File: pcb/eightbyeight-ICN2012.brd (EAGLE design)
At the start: 60 x 60 mm, 136 parts, among them CON1 USB_MICROSMT+THRUHULE, Q1 16MHz, SW1 SWITCH_SPDT, SW2 BRIGHTNESS, U1 MK20DN64VFM5, U2 ICN2026, U4 ICN2026, U5 MIC5219 3.3V, U6 ESP_WROOM_02, U8 MMA8653FC

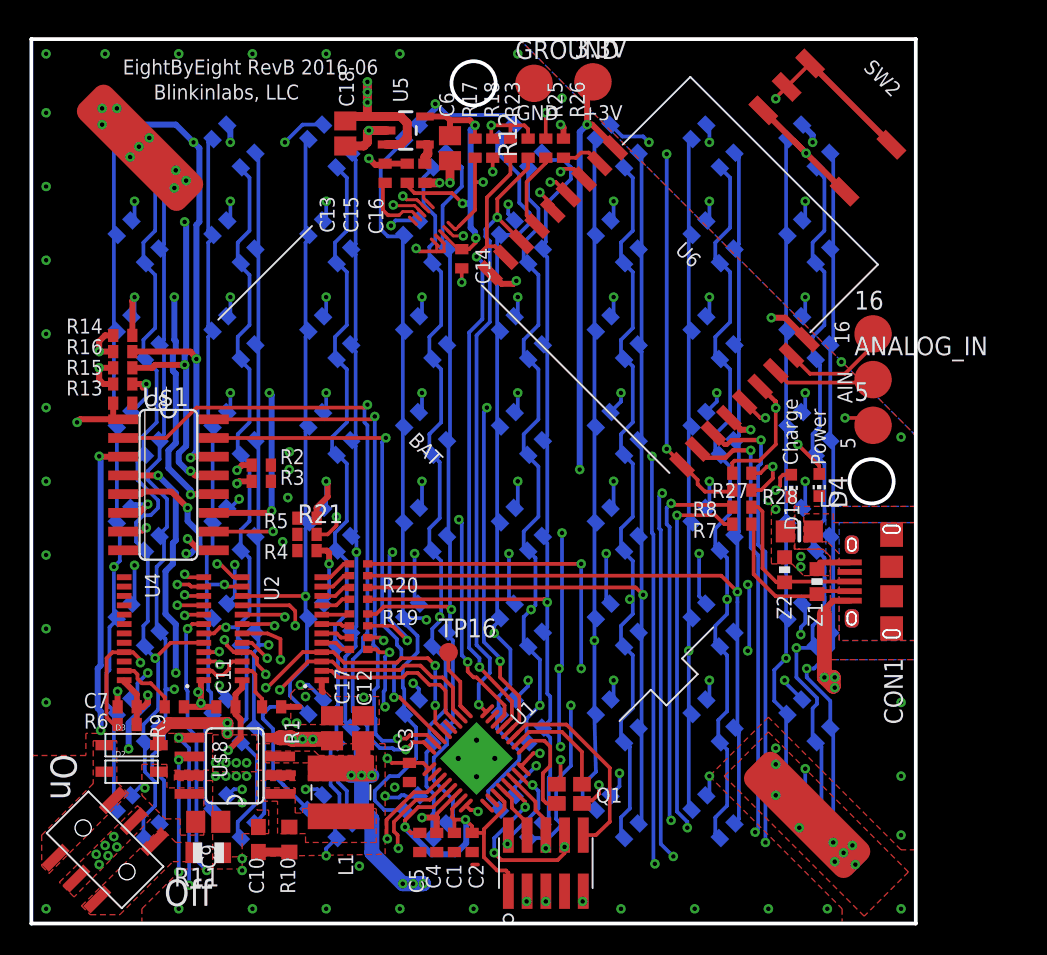
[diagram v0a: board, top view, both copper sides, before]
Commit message: Update ICN2012 version with new accelerometer
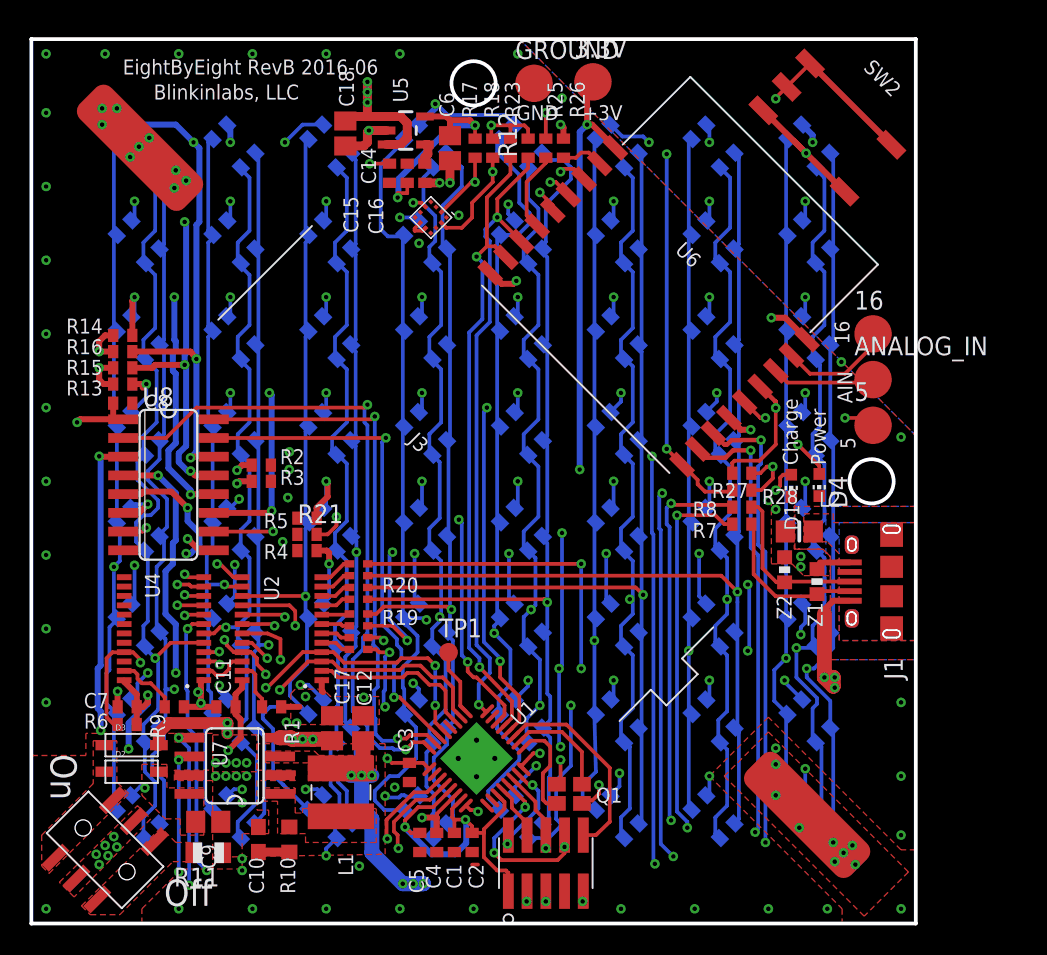
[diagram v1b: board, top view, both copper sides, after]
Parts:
- removed C13: 100nF, adafruit:C0402
- removed U$1: ICN2012, blinkinlabs:SO16
- added U3: QMA6981, DevicesToMerge:LGA2X2MM
- R21: value 2k 1% -> 10k
- U1: value MK20DN64VFM5 -> MK20DN32VFM5
- U8: value MMA8653FC -> ICN2012; device teensy_adapter:VFDFN-10 -> blinkinlabs:SO16
- moved U8 24.8 mm to (9.30, 30.4), turned to 270 degrees
- moved C14 7.59 mm to (24.3, 50.9), turned to 90 degrees
- renumbered BAT to J3, CON1 to J1, TP16 to TP1, U$2 to J2, U$8 to U7
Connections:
- removed net ACC_INT1: U6.IO13, U8.P$3
- removed net N$5: C13.1, U8.P$4
- new net ADC_INT1: U3.5, U6.IO13
- new net INT2: U3.6
- net +3V3: now also U3.3, U3.7; no longer U8.P$1, U8.P$8
- net +5V: now also U8.1, U8.9; no longer U$1.1, U$1.9
- net 1ROW0: now also U8.3; no longer U$1.3
- net 1ROW1: now also U8.4; no longer U$1.4
- net 1ROW2: now also U8.5; no longer U$1.5
- net 1ROW3: now also U8.6; no longer U$1.6
- net 1ROW4: now also U8.11; no longer U$1.11
- net 1ROW5: now also U8.12; no longer U$1.12
- net 1ROW6: now also U8.13; no longer U$1.13
- net 1ROW7: now also U8.14; no longer U$1.14
- net GND: now also U3.1, U3.4, U3.8, U3.9, U8.8; no longer C13.2, U$1.8, U8.P$6, U8.P$7, U8.P$9
- net I2C_SCL: now also U3.12; no longer U8.P$2
- net I2C_SDA: now also U3.2; no longer U8.P$10
- net LED_HS_EN: now also U8.7; no longer U$1.7
- net LED_OE: now also U8.10; no longer U$1.10
- net LED_ROW_A: now also U8.15; no longer U$1.15
- net LED_ROW_B: now also U8.16; no longer U$1.16
- net LED_ROW_C: now also U8.2; no longer U$1.2
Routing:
- net ACC_INT1: track 14.2 -> 0.00 mm, vias 2 -> 0
- net ADC_INT1: track 0.00 -> 11.4 mm, vias 0 -> 2
- net +3V3: track 83.2 -> 75.9 mm, vias 8 -> 7
- net N$5: track 4.61 -> 0.00 mm
- net GND: track 87.8 -> 90.7 mm, vias 90 -> 89
- net I2C_SCL: track 16.2 -> 13.7 mm, vias 3 -> 2
- net 1ROW6: track 82.9 -> 83.9 mm
- net I2C_SDA: track 12.5 -> 11.5 mm

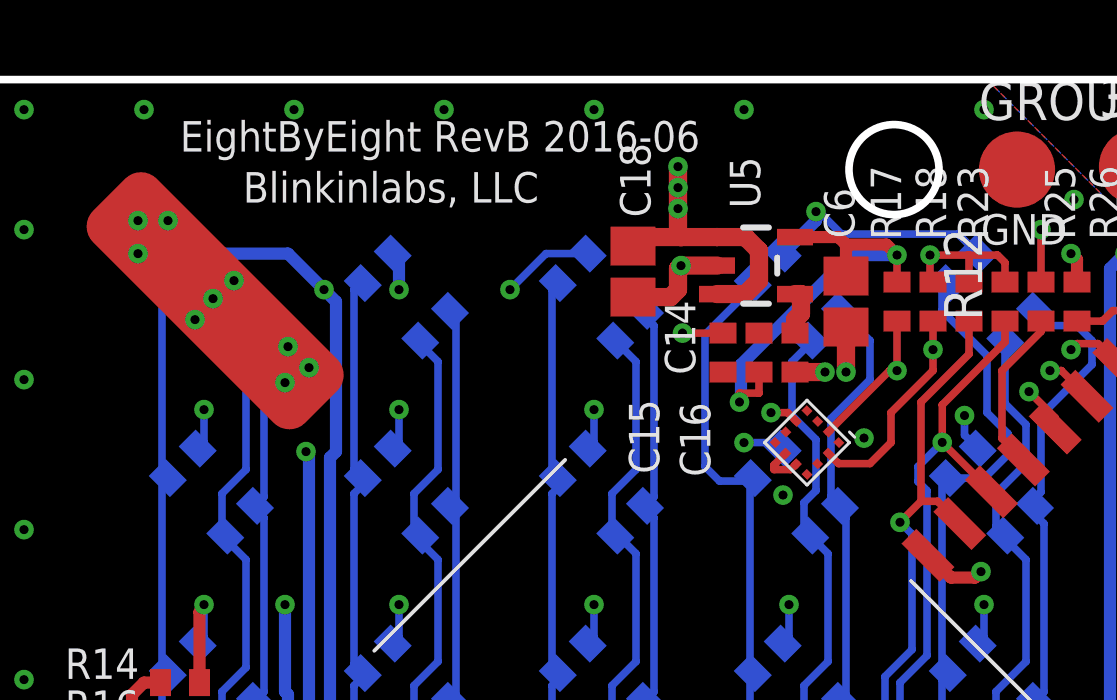
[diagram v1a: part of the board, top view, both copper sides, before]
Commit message: Finish laying out accelerometer, minor updates to part values/reference designators
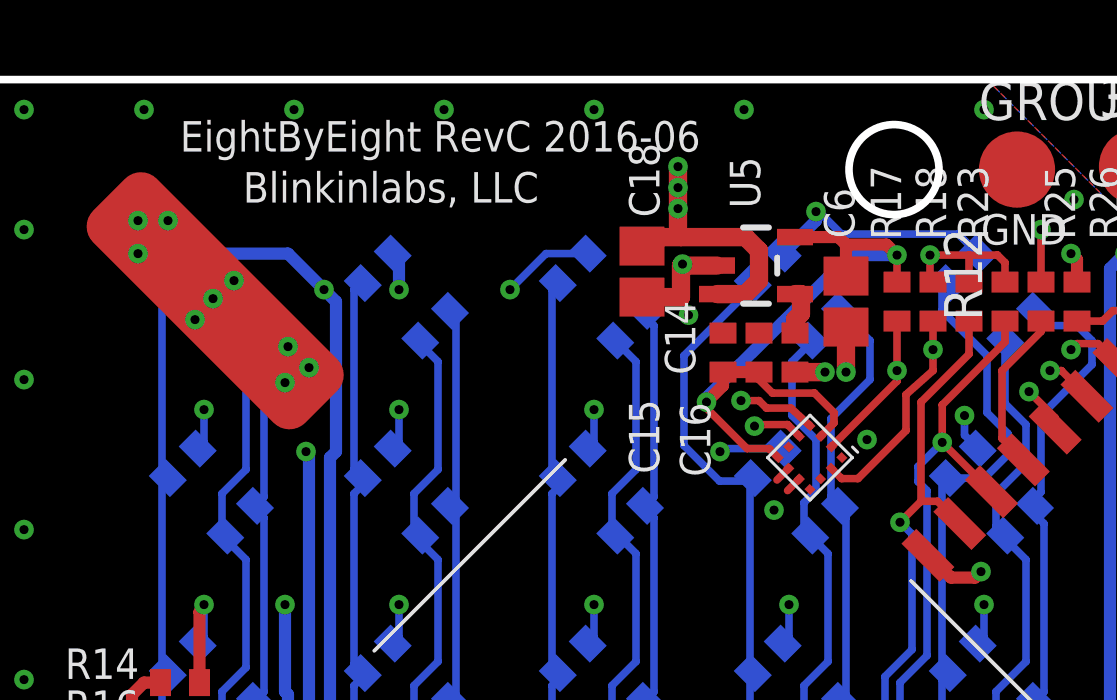
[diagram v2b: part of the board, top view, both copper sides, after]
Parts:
- C14: value 100nF -> 1uF
- moved U3 0.51 mm to (27.2, 47.4)
- moved C18 0.30 mm to (21.6, 53.6)
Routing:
- net GND: track 90.7 -> 81.1 mm, vias 89 -> 90
- net +3V3: track 75.9 -> 84.6 mm
- net ADC_INT1: track 11.4 -> 12.9 mm
- net BCOL3: track 68.2 -> 68.8 mm
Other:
- board text added: "EightByEight RevC 2016-06"
- board text removed: "EightByEight RevB 2016-06"

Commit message: Update board TODOs
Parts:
- C16: value 470pF -> 47pF
- C6: value 10uF -> 20uF
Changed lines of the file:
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@@
 <attribute name="VALUE" x="11.514" y="5.389" size="1.016" layer="27" rot="R270"/>
 </element>
-<element name="C6" library="adafruit" package="C0805" value="10uF" x="28.4" y="52.6" smashed="yes" rot="R270">
+<element name="C6" library="adafruit" package="C0805" value="20uF" x="28.4" y="52.6" smashed="yes" rot="R270">
 <attribute name="NAME" x="28.684" y="54.711" size="1.016" layer="25" rot="R90"/>
 <attribute name="VALUE" x="28.686" y="54.711" size="1.016" layer="27" rot="R90"/>
@@
 <attribute name="VALUE" x="25.5905" y="55.7475" size="1.016" layer="27" rot="R90"/>
 </element>
-<element name="C16" library="adafruit" package="C0402" value="470pF" x="26.7" y="50.9" smashed="yes" rot="R270">
+<element name="C16" library="adafruit" package="C0402" value="47pF" x="26.7" y="50.9" smashed="yes" rot="R270">
 <attribute name="NAME" x="22.862" y="49.235" size="1.016" layer="25" rot="R270"/>
 <attribute name="VALUE" x="22.895" y="49.235" size="1.016" layer="27" rot="R270"/>

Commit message: Silkscreen tweaks to pcbs
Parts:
- U2, U4: value ICN2026 -> ICN2027
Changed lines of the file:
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@@
 <layers>
 <layer number="1" name="Top" color="12" fill="1" visible="yes" active="yes"/>
-<layer number="2" name="GND" color="1" fill="1" visible="no" active="yes"/>
+<layer number="2" name="GND" color="1" fill="1" visible="yes" active="yes"/>
 <layer number="3" name="Route3" color="4" fill="3" visible="no" active="no"/>
 <layer number="4" name="Route4" color="1" fill="4" visible="no" active="no"/>
@@
 </autorouter>
 <elements>
-<element name="U2" library="blinkinlabs" package="SSOP24-150" value="ICN2026" x="17" y="19.9995" smashed="yes" rot="R180">
+<element name="U2" library="blinkinlabs" package="SSOP24-150" value="ICN2027" x="17" y="19.9995" smashed="yes" rot="R180">
 <attribute name="NAME" x="15.79033125" y="23.61224375" size="1.016" layer="25" rot="R270"/>
 <attribute name="VALUE" x="17.300503125" y="23.6" size="1.016" layer="27" rot="R270"/>
@@
 <attribute name="VALUE" x="17.235" y="28.032" size="1.016" layer="27" rot="R180"/>
 </element>
-<element name="U4" library="blinkinlabs" package="SSOP24-150" value="ICN2026" x="9" y="20" smashed="yes" rot="R180">
+<element name="U4" library="blinkinlabs" package="SSOP24-150" value="ICN2027" x="9" y="20" smashed="yes" rot="R180">
 <attribute name="NAME" x="7.7" y="23.8" size="1.016" layer="25" rot="R270"/>
 <attribute name="VALUE" x="9.3" y="23.8" size="1.016" layer="27" rot="R270"/>

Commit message: Add (nonworking) RevC design
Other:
- board text added: "3.3V"
- board text removed: "+3V"
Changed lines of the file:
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@@
 <text x="55.9" y="32.2" size="1.016" layer="21" rot="R90">5</text>
 <text x="32.9" y="54.5" size="1.016" layer="21">GND</text>
-<text x="37.4" y="54.5" size="1.016" layer="21">+3V</text>
+<text x="36.6" y="54.5" size="1.016" layer="21">3.3V</text>
 <rectangle x1="35.663328125" y1="4.127471875" x2="35.747146875" y2="4.169890625" layer="200"/>
 <rectangle x1="35.620146875" y1="4.169890625" x2="35.790328125" y2="4.212053125" layer="200"/>
